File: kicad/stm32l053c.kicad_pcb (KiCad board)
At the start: 2 copper layers, 90 x 70 mm, 55 parts, among them J1 Water_Level, J2 Motion, J3 Door, J4 Door_Led, J6 Pump, J7 BATTERY, P1 SWD, Q1 Q_NMOS_GSD, Q2 Q_PMOS_GSD, U1 MCP1703A-5002_SOT223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

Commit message: All connected
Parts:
- R16, R17, R18: moved to F.Cu
- moved D2 74.5 mm to (169.0, 84.0), turned to 90 degrees
- moved R16 63.3 mm to (162.0, 82.0), turned to 0 degrees
- moved R17 59.9 mm to (162.0, 79.0), turned to 0 degrees
- moved R18 56.7 mm to (162.0, 76.0), turned to 0 degrees
- moved R19 1.70 mm to (117.5, 60.1)
- moved R20 1.70 mm to (115.0, 60.1)
- moved R5 1.70 mm to (115.1, 55.8)
- moved J6 0.71 mm to (169.0, 104.0), turned to 90 degrees
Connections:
- U2 pad 16: DOOR_LED -> PUMP
- U2 pad 2: PUMP -> DOOR_LED
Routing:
- net Earth: track 247.5 -> 351.6 mm, vias 5 -> 7
- net MOTION: track 4.64 -> 87.8 mm, vias 0 -> 3
- net DOOR: track 3.60 -> 81.4 mm, vias 0 -> 3
- net DOOR_LED: track 0.00 -> 63.7 mm, vias 0 -> 3
- net PUMP: track 0.00 -> 32.0 mm
- net DIO0: track 1.45 -> 19.6 mm, vias 0 -> 2
- net LED_RED: track 0.00 -> 8.01 mm
- net LED_BLUE: track 0.00 -> 7.59 mm
- net LED_GREEN: track 0.00 -> 6.95 mm
- net Net-(D2-Pad4): track 0.00 -> 6.18 mm
- net Net-(D2-Pad2): track 0.00 -> 6.18 mm
- net Net-(D2-Pad3): track 0.00 -> 6.00 mm
- net +3V3: track 224.1 -> 219.5 mm
- net Net-(R20-Pad2): track 0.00 -> 3.53 mm
- net Net-(R19-Pad2): track 0.00 -> 3.48 mm
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- added copper zone on B.Cu, net Earth
- added copper zone on F.Cu, net Earth
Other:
- outline, holes or cut-outs redrawn

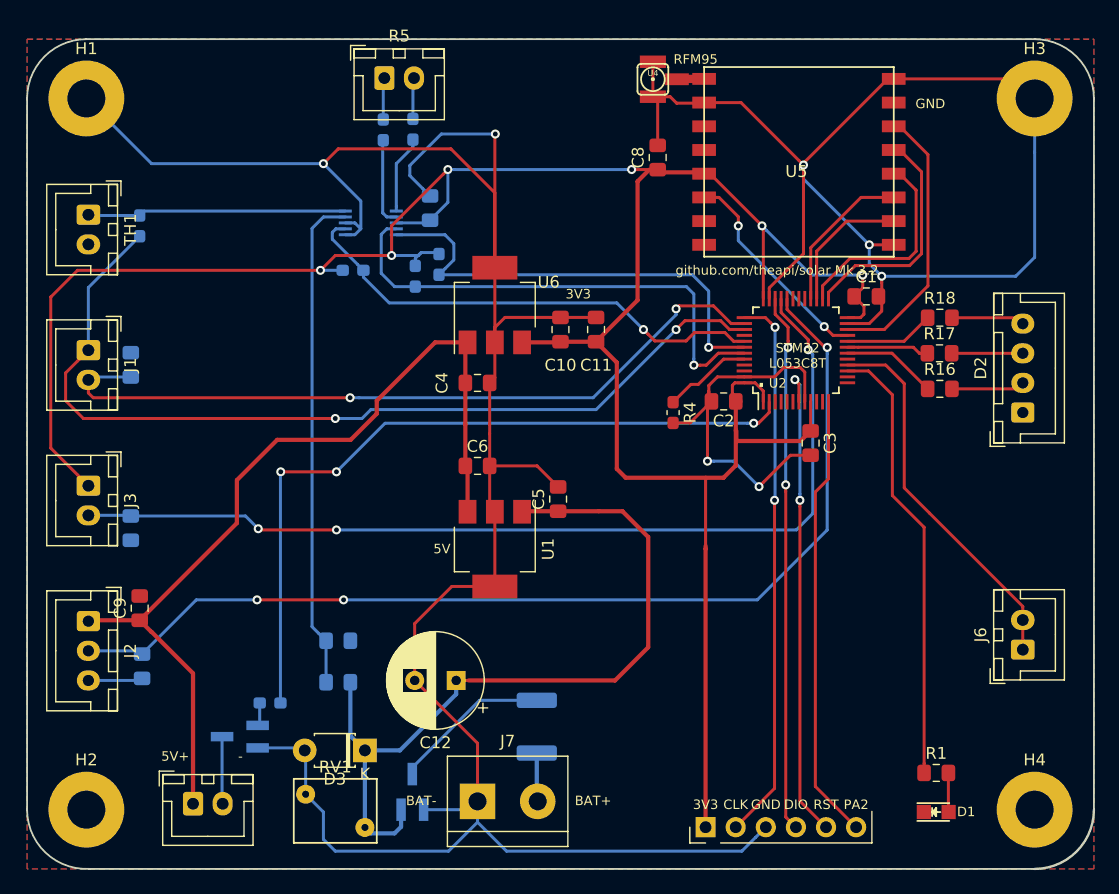
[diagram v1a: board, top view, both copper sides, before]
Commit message: Power switch
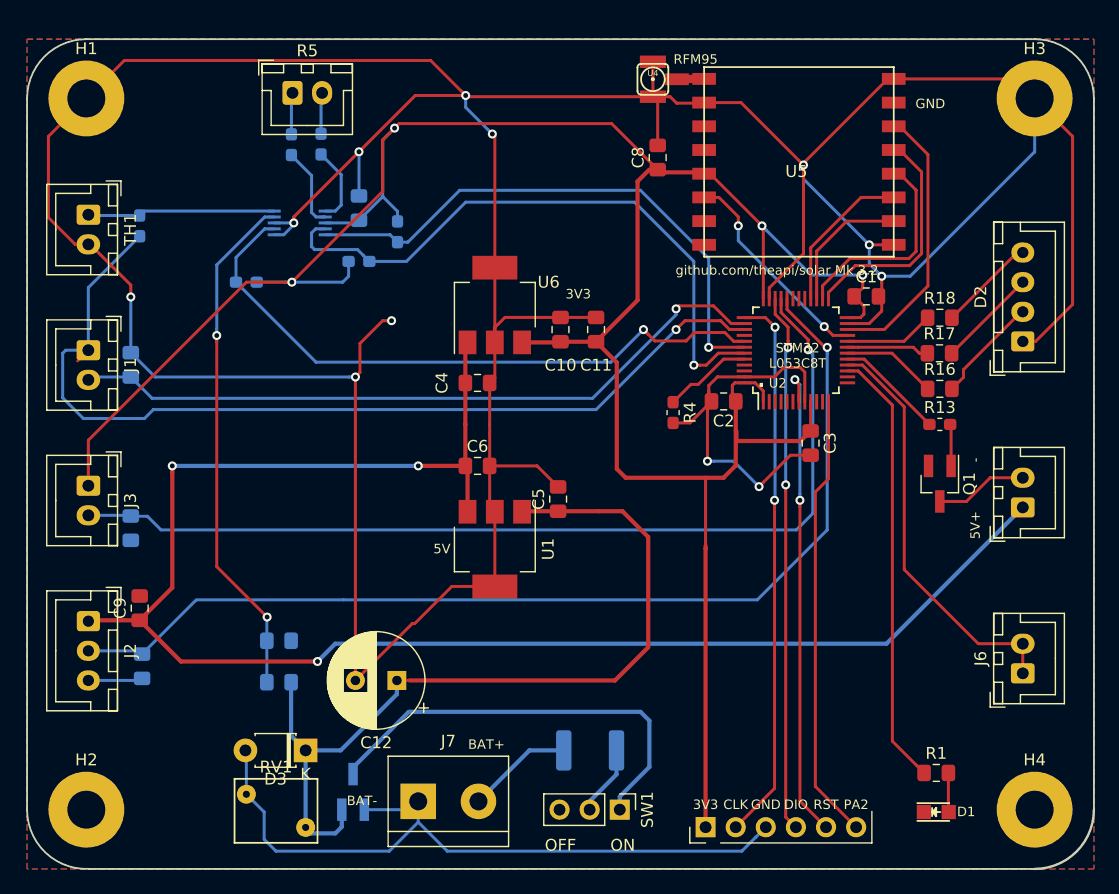
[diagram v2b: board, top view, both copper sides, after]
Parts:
- added SW1: SW_Push_SPDT, Connector_PinHeader_2.54mm:PinHeader_1x03_P2.54mm_Vertical, F.Cu at (135.0, 117.5)
- Q1, R13: moved to F.Cu
- moved J4 74.3 mm to (169.0, 92.0), turned to 90 degrees
- moved Q1 62.8 mm to (162.0, 90.0), turned to 270 degrees
- moved R13 61.2 mm to (162.0, 85.0), turned to 0 degrees
- moved R10 9.06 mm to (103.5, 73.0), turned to 180 degrees
- moved R19 7.85 mm to (109.8, 61.4)
- moved R20 7.85 mm to (107.3, 61.4)
- moved R5 7.85 mm to (107.4, 57.0)
- moved C7 6.00 mm to (113.0, 66.8)
- moved D2 6.00 mm to (169.0, 78.0)
- moved U3 6.00 mm to (108.0, 68.0)
- moved C12 5.00 mm to (116.2, 106.6)
- moved D3 5.00 mm to (108.5, 112.5)
- moved J7 5.00 mm to (118.0, 116.8)
- moved Q2 5.00 mm to (112.5, 116.0)
- moved R8 5.00 mm to (106.2, 106.8)
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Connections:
- Q2 pad 3: Net-(F1-Pad1) -> Net-(Q2-Pad3)
- U2 pad 10: Net-(U2-Pad10) -> (no net)
- U2 pad 11: Net-(U2-Pad11) -> (no net)
- U2 pad 13: USART2_RX -> (no net)
- U2 pad 14: Net-(U2-Pad14) -> (no net)
- U2 pad 17: Net-(U2-Pad17) -> DOOR_LED
- U2 pad 2: DOOR_LED -> (no net)
- U2 pad 29: Net-(U2-Pad29) -> (no net)
- U2 pad 3: Net-(U2-Pad3) -> (no net)
- U2 pad 30: Net-(U2-Pad30) -> (no net)
- U2 pad 31: Net-(U2-Pad31) -> (no net)
- U2 pad 4: Net-(U2-Pad4) -> (no net)
- U2 pad 40: Net-(U2-Pad40) -> (no net)
- U2 pad 45: Net-(U2-Pad45) -> (no net)
- U2 pad 46: Net-(U2-Pad46) -> (no net)
- U2 pad 5: Net-(U2-Pad5) -> (no net)
- U2 pad 6: Net-(U2-Pad6) -> (no net)
- U5 pad 11: Net-(U5-Pad11) -> (no net)
- U5 pad 12: Net-(U5-Pad12) -> (no net)
- U5 pad 15: Net-(U5-Pad15) -> (no net)
- U5 pad 16: Net-(U5-Pad16) -> (no net)
- U5 pad 7: Net-(U5-Pad7) -> (no net)
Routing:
- net Earth: track 351.6 -> 454.7 mm, vias 7 -> 12
- net +5V: track 76.3 -> 139.0 mm, vias 0 -> 3
- net DOOR_LED: track 63.7 -> 9.20 mm, vias 3 -> 0
- net Net-(Q2-Pad3): track 0.00 -> 36.3 mm
- net ADC_RDY: track 41.1 -> 54.1 mm
- net I2C1_SDA: track 42.5 -> 52.8 mm
- net I2C1_SCL: track 39.4 -> 47.3 mm
- net Net-(F1-Pad1): track 13.4 -> 5.94 mm
- net WATER_TEMP: track 22.2 -> 16.2 mm
- net /BATT: track 66.7 -> 71.7 mm
- net +BATT: track 4.11 -> 9.09 mm
- net WATER_LEVEL: track 64.4 -> 60.3 mm, vias 2 -> 1
- net PUMP: track 32.0 -> 35.1 mm
- net Net-(D2-Pad2): track 6.18 -> 9.05 mm
- net SENSOR_PWR: track 78.1 -> 80.7 mm, vias 2 -> 1
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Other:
- board text added: "OFF"
- board text added: "ON"

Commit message: Labels
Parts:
- D2: value LED_CRGB -> RGB LED
- J4: value Door_Led -> DOOR LED
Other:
- board text added: "Current Sensor"
- board text added: "Door Switch"
- board text added: "Motion Sensor"
- board text added: "Power Max 16V"
- board text added: "Pump Switch"
- board text added: "Water Level"
- board text added: "Water Temperature"
- board text added: "github.com/theapi/gard_hw v1.0"
- board text removed: "github.com/theapi/solar Mk 3.2"

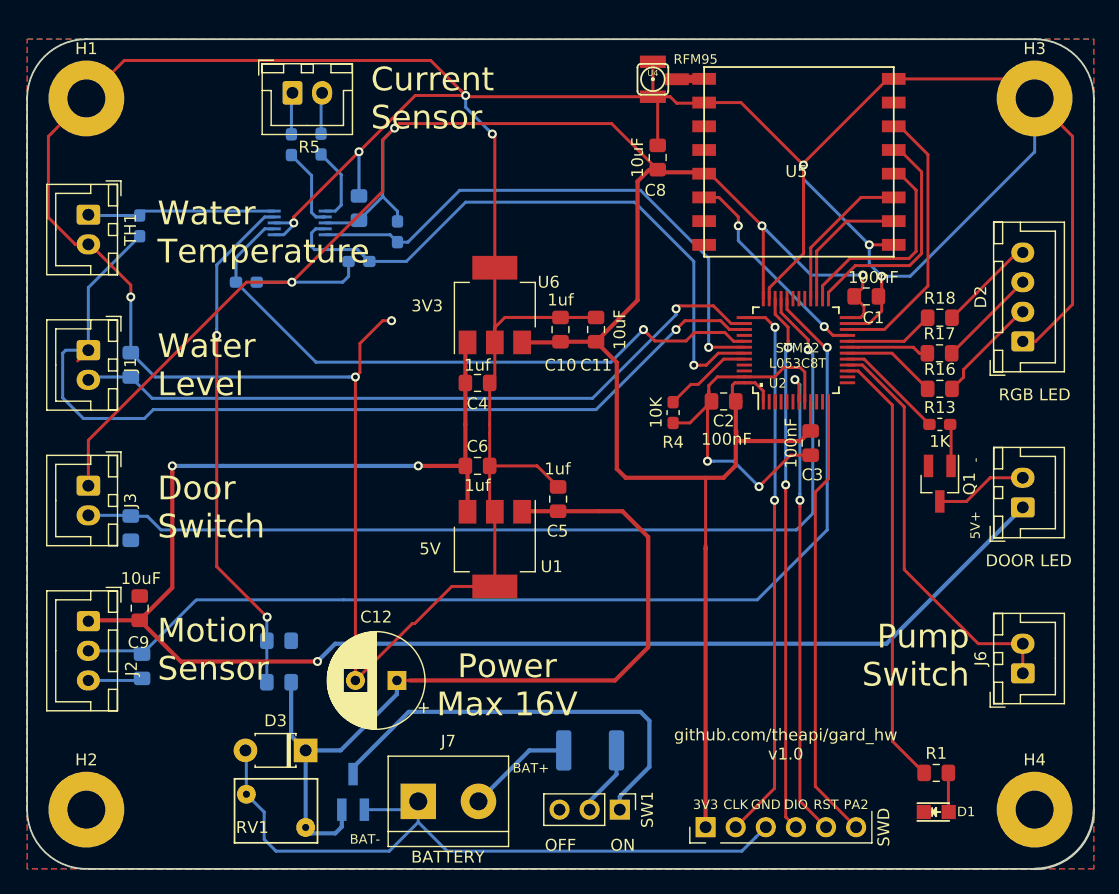
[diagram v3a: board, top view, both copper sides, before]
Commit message: Altenate 5V regulator
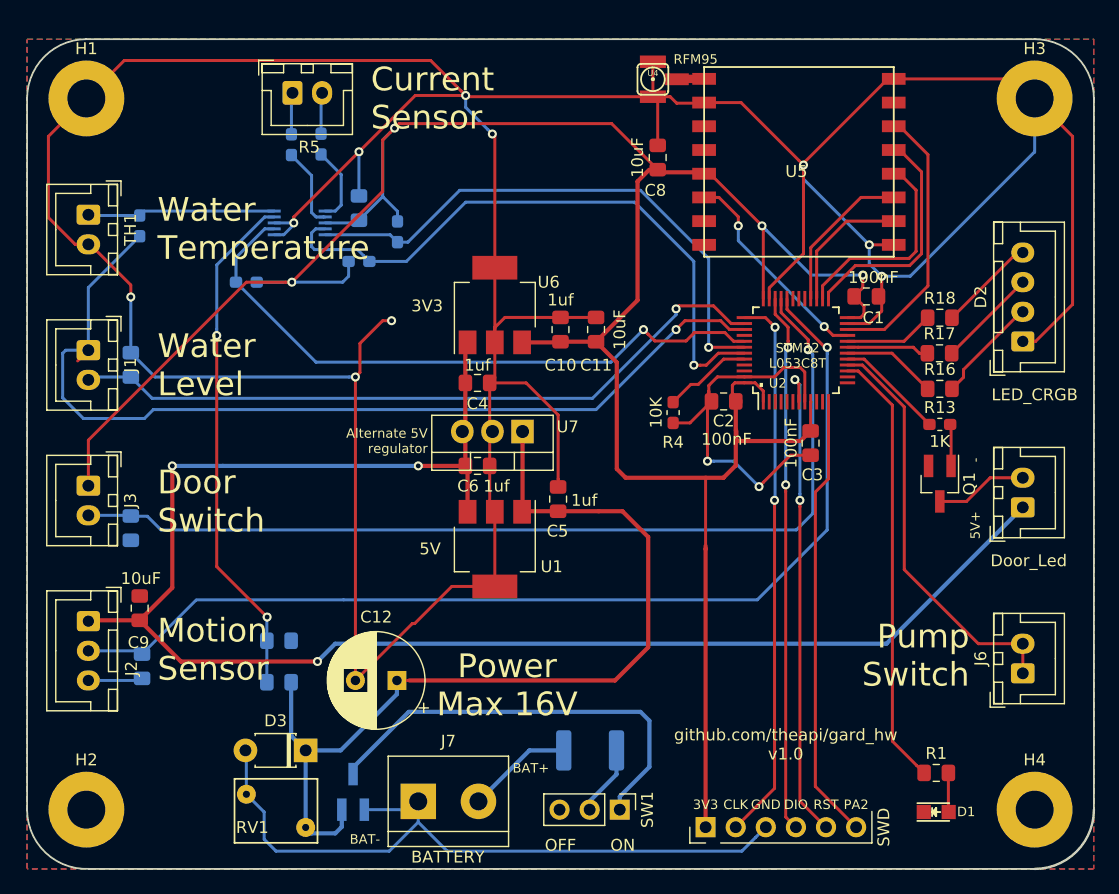
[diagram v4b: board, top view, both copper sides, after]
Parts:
- added U7: LP2954_TO220, Package_TO_SOT_THT:TO-220-3_Vertical, F.Cu at (126.8, 85.6)
- D2: value RGB LED -> LED_CRGB
- J4: value DOOR LED -> Door_Led
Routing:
- net /BATT: track 71.7 -> 78.5 mm
- net Earth: track 454.7 -> 461.2 mm
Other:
- board text added: "Alternate 5V regulator"
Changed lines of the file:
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@@
   (general
     (thickness 1.6)
-    (drawings 42)
-    (tracks 521)
+    (drawings 43)
+    (tracks 525)
     (zones 0)
-    (modules 56)
+    (modules 57)
     (nets 45)
   )
@@
       (effects (font (size 1 1) (thickness 0.15)))
     )
-    (fp_text value "RGB LED " (at -4.5 1 180) (layer F.SilkS)
+    (fp_text value LED_CRGB (at -4.5 1 180) (layer F.SilkS)
       (effects (font (size 1 1) (thickness 0.15)))
     )
@@
       (effects (font (size 1 1) (thickness 0.15)))
     )
-    (fp_text value "DOOR LED" (at -4.5 0.5 180) (layer F.SilkS)
+    (fp_text value Door_Led (at -4.5 0.5 180) (layer F.SilkS)
       (effects (font (size 1 1) (thickness 0.15)))
     )
@@
       (effects (font (size 1 1) (thickness 0.15)))
     )
-    (fp_text value 1uf (at 2.55 -0.05 180) (layer F.SilkS)
+    (fp_text value 1uf (at -0.1 2.2 180) (layer F.SilkS)
       (effects (font (size 1 1) (thickness 0.15)))
     )
@@
     (tags "capacitor handsolder")
     (attr smd)
-    (fp_text reference C6 (at 0 -1.65) (layer F.SilkS)
+    (fp_text reference C6 (at -0.8 1.7) (layer F.SilkS)
       (effects (font (size 1 1) (thickness 0.15)))
     )
-    (fp_text value 1uf (at 0 1.65) (layer F.SilkS)
+    (fp_text value 1uf (at 1.6 1.7) (layer F.SilkS)
       (effects (font (size 1 1) (thickness 0.15)))
     )
@@
     )
   )
+  (module Package_TO_SOT_THT:TO-220-3_Vertical (layer F.Cu)
+    (at 126.8 85.6 180)
+    (descr "TO-220-3, Vertical, RM 2.54mm, see https://www.vishay.com/docs/66542/to-220-1.pdf")
+    (tags "TO-220-3 Vertical RM 2.54mm")
+    (fp_text reference U7 (at -3.8 0.4 180) (layer F.SilkS)
+      (effects (font (size 1 1) (thickness 0.15)))
+    )
+    (fp_text value LP2954_TO220 (at 2.54 2.5 180) (layer F.Fab)
+      (effects (font (size 1 1) (thickness 0.15)))
+    )
+    (fp_line (start -2.46 -3.15) (end -2.46 1.25) (layer F.Fab) (width 0.1))
+    (fp_line (start -2.46 1.25) (end 7.54 1.25) (layer F.Fab) (width 0.1))
+    (fp_line (start 7.54 1.25) (end 7.54 -3.15) (layer F.Fab) (width 0.1))
+    (fp_line (start 7.54 -3.15) (end -2.46 -3.15) (layer F.Fab) (width 0.1))
+    (fp_line (start -2.46 -1.88) (end 7.54 -1.88) (layer F.Fab) (width 0.1))
+    (fp_line (start 0.69 -3.15) (end 0.69 -1.88) (layer F.Fab) (width 0.1))
+    (fp_line (start 4.39 -3.15) (end 4.39 -1.88) (layer F.Fab) (width 0.1))
+    (fp_line (start -2.58 -3.27) (end 7.66 -3.27) (layer F.SilkS) (width 0.12))
+    (fp_line (start -2.58 1.371) (end 7.66 1.371) (layer F.SilkS) (width 0.12))
+    (fp_line (start -2.58 -3.27) (end -2.58 1.371) (layer F.SilkS) (width 0.12))
+    (fp_line (start 7.66 -3.27) (end 7.66 1.371) (layer F.SilkS) (width 0.12))
+    (fp_line (start -2.58 -1.76) (end 7.66 -1.76) (layer F.SilkS) (width 0.12))
+    (fp_line (start 0.69 -3.27) (end 0.69 -1.76) (layer F.SilkS) (width 0.12))
+    (fp_line (start 4.391 -3.27) (end 4.391 -1.76) (layer F.SilkS) (width 0.12))
+    (fp_line (start -2.71 -3.4) (end -2.71 1.51) (layer F.CrtYd) (width 0.05))
+    (fp_line (start -2.71 1.51) (end 7.79 1.51) (layer F.CrtYd) (width 0.05))
+    (fp_line (start 7.79 1.51) (end 7.79 -3.4) (layer F.CrtYd) (width 0.05))
+    (fp_line (start 7.79 -3.4) (end -2.71 -3.4) (layer F.CrtYd) (width 0.05))
+    (fp_text user %R (at 2.54 -4.27 180) (layer F.Fab)
+      (effects (font (size 1 1) (thickness 0.15)))
+    )
+    (pad 1 thru_hole rect (at 0 0 180) (size 1.905 2) (drill 1.1) (layers *.Cu *.Mask)
+      (net 38 /BATT))
+    (pad 2 thru_hole oval (at 2.54 0 180) (size 1.905 2) (drill 1.1) (layers *.Cu *.Mask)
+      (net 1 Earth))
+    (pad 3 thru_hole oval (at 5.08 0 180) (size 1.905 2) (drill 1.1) (layers *.Cu *.Mask)
+      (net 34 +5V))
+    (model ${KISYS3DMOD}/Package_TO_SOT_THT.3dshapes/TO-220-3_Vertical.wrl
+      (at (xyz 0 0 0))
+      (scale (xyz 1 1 1))
+      (rotate (xyz 0 0 0))
+    )
+  )
+  (gr_text "Alternate 5V\nregulator" (at 118.8 86.4) (layer F.SilkS)
+    (effects (font (size 0.8 0.8) (thickness 0.15)) (justify right))
+  )
   (gr_text 3V3 (at 118.75 75) (layer F.SilkS)
     (effects (font (size 1 1) (thickness 0.25)))
@@
     (effects (font (size 2 2) (thickness 0.5)) (justify left))
   )
-  (gr_text "Door\nSwitch" (at 96 92) (layer F.SilkS)
+  (gr_text "Door\nSwitch" (at 96 91.5) (layer F.SilkS)
     (effects (font (size 2 2) (thickness 0.5)) (justify left))
   )
@@
     (effects (font (size 2 2) (thickness 0.5)) (justify left))
   )
-  (gr_text "Water\nTemperature" (at 96 68.8) (layer F.SilkS)
+  (gr_text "Water\nTemperature" (at 96 68.5) (layer F.SilkS)
     (effects (font (size 2 2) (thickness 0.5)) (justify left))
   )
@@
   (segment (start 124.46 81.065) (end 124.025 81.5) (width 0.254) (layer F.Cu) (net 1))
   (segment (start 124.46 78.08) (end 124.46 81.065) (width 0.254) (layer F.Cu) (net 1))
-  (segment (start 124.025 81.5) (end 124.025 85) (width 0.254) (layer F.Cu) (net 1))
   (segment (start 124.025 85.8) (end 124.025 88.5) (width 0.254) (layer F.Cu) (net 1))
-  (segment (start 124.025 85) (end 124.025 85.8) (width 0.254) (layer F.Cu) (net 1))
   (segment (start 124.025 91.935) (end 124.46 92.37) (width 0.254) (layer F.Cu) (net 1))
   (segment (start 124.025 88.5) (end 124.025 91.935) (width 0.254) (layer F.Cu) (net 1))
@@
   (segment (start 157.099994 75.436599) (end 157.099994 73.038815) (width 0.254) (layer F.Cu) (net 1))
   (segment (start 154.21 76.49) (end 156.046593 76.49) (width 0.254) (layer F.Cu) (net 1))
-  (segment (start 128.025 88.5) (end 124.025 88.5) (width 0.254) (layer F.Cu) (net 1))
-  (segment (start 129.8 90.275) (end 128.025 88.5) (width 0.254) (layer F.Cu) (net 1))
   (segment (start 142.065 57.9) (end 142.115 57.85) (width 0.254) (layer F.Cu) (net 1))
   (segment (start 139.8 57.9) (end 142.065 57.9) (width 0.254) (layer F.Cu) (net 1))
@@
   (segment (start 115 76.25) (end 115.75 76.25) (width 0.254) (layer F.Cu) (net 1))
   (segment (start 113.080999 78.169001) (end 115 76.25) (width 0.254) (layer F.Cu) (net 1))
+  (segment (start 124.025 85) (end 124.025 85.8) (width 0.254) (layer F.Cu) (net 1) (status 1000000))
+  (segment (start 124.025 81.5) (end 124.025 85) (width 0.254) (layer F.Cu) (net 1) (status 1000000))
+  (segment (start 129.8 89.6) (end 129.8 90.275) (width 0.254) (layer F.Cu) (net 1))
+  (segment (start 127.1 81.5) (end 129.8 84.2) (width 0.254) (layer F.Cu) (net 1))
+  (segment (start 129.8 84.2) (end 129.8 89.6) (width 0.254) (layer F.Cu) (net 1))
+  (segment (start 124.025 81.5) (end 127.1 81.5) (width 0.254) (layer F.Cu) (net 1))
   (via (at 148.1 76.8) (size 0.762) (drill 0.4064) (layers F.Cu B.Cu) (net 2))
   (segment (start 145.51 75.99) (end 147.29 75.99) (width 0.254) (layer F.Cu) (net 2))
@@
   (segment (start 122.16 88.685) (end 121.975 88.5) (width 0.254) (layer F.Cu) (net 34))
   (segment (start 122.16 92.37) (end 122.16 88.685) (width 0.3556) (layer F.Cu) (net 34))
-  (segment (start 121.975 88.5) (end 121.975 85) (width 0.3556) (layer F.Cu) (net 34))
-  (segment (start 121.975 85) (end 121.975 81.5) (width 0.3556) (layer F.Cu) (net 34))
   (segment (start 121.975 78.265) (end 122.16 78.08) (width 0.254) (layer F.Cu) (net 34))
   (segment (start 121.975 81.5) (end 121.975 78.265) (width 0.3556) (layer F.Cu) (net 34))
@@
   (segment (start 94.5 101.525) (end 97.249998 98.775002) (width 0.3556) (layer F.Cu) (net 34))
   (via (at 97.249998 88.5) (size 0.762) (drill 0.4064) (layers F.Cu B.Cu) (net 34))
+  (segment (start 121.975 88.5) (end 121.975 85) (width 0.3556) (layer F.Cu) (net 34) (status 1000000))
+  (segment (start 121.975 85) (end 121.975 81.5) (width 0.3556) (layer F.Cu) (net 34) (status 1000000))
   (segment (start 168.875 75.5) (end 169 75.5) (width 0.254) (layer F.Cu) (net 35))
   (segment (start 164 80.375) (end 168.875 75.5) (width 0.254) (layer F.Cu) (net 35))
@@
   (segment (start 134.6 106.6) (end 137.4 103.8) (width 0.3556) (layer F.Cu) (net 38))
   (segment (start 137.4 103.8) (end 137.4 94.5) (width 0.3556) (layer F.Cu) (net 38))
+  (segment (start 126.8 92.33) (end 126.76 92.37) (width 0.3556) (layer F.Cu) (net 38))
+  (segment (start 126.8 85.6) (end 126.8 92.33) (width 0.3556) (layer F.Cu) (net 38))
   (segment (start 107.3 57.12) (end 107.39 57.03) (width 0.254) (layer B.Cu) (net 39))
   (segment (start 107.3 60.525) (end 107.3 57.12) (width 0.254) (layer B.Cu) (net 39))
